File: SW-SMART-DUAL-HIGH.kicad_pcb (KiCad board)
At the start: 2 copper layers, 72 x 69 mm, 42 parts, among them IC1 MCP1416, J1 SWLINK, J2 USART1, SW1 BTS50010-1TAD, SW2 VNB35N07xx-E, U1 STM32G0B1KBTx, U4 MCP2562-E-SN

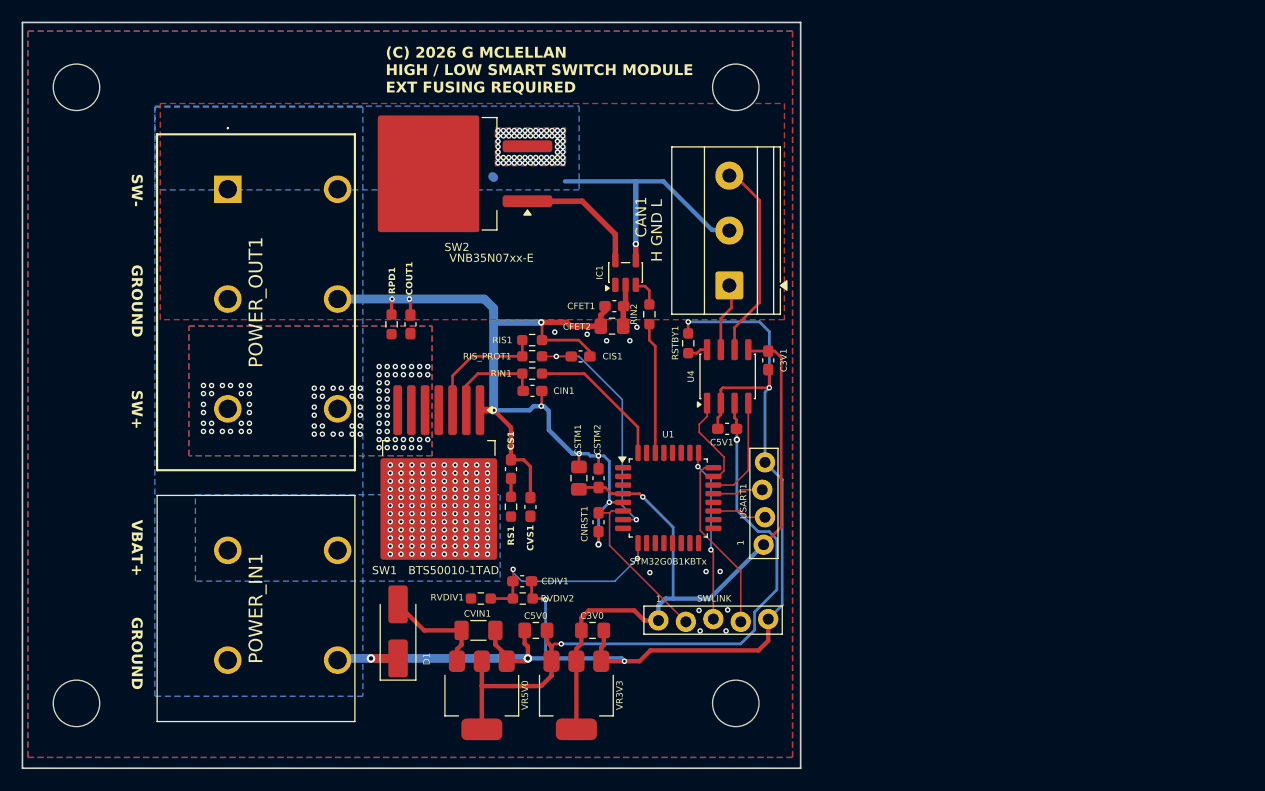
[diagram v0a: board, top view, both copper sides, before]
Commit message: lots of rework to adapt previous layout to new switch configuration
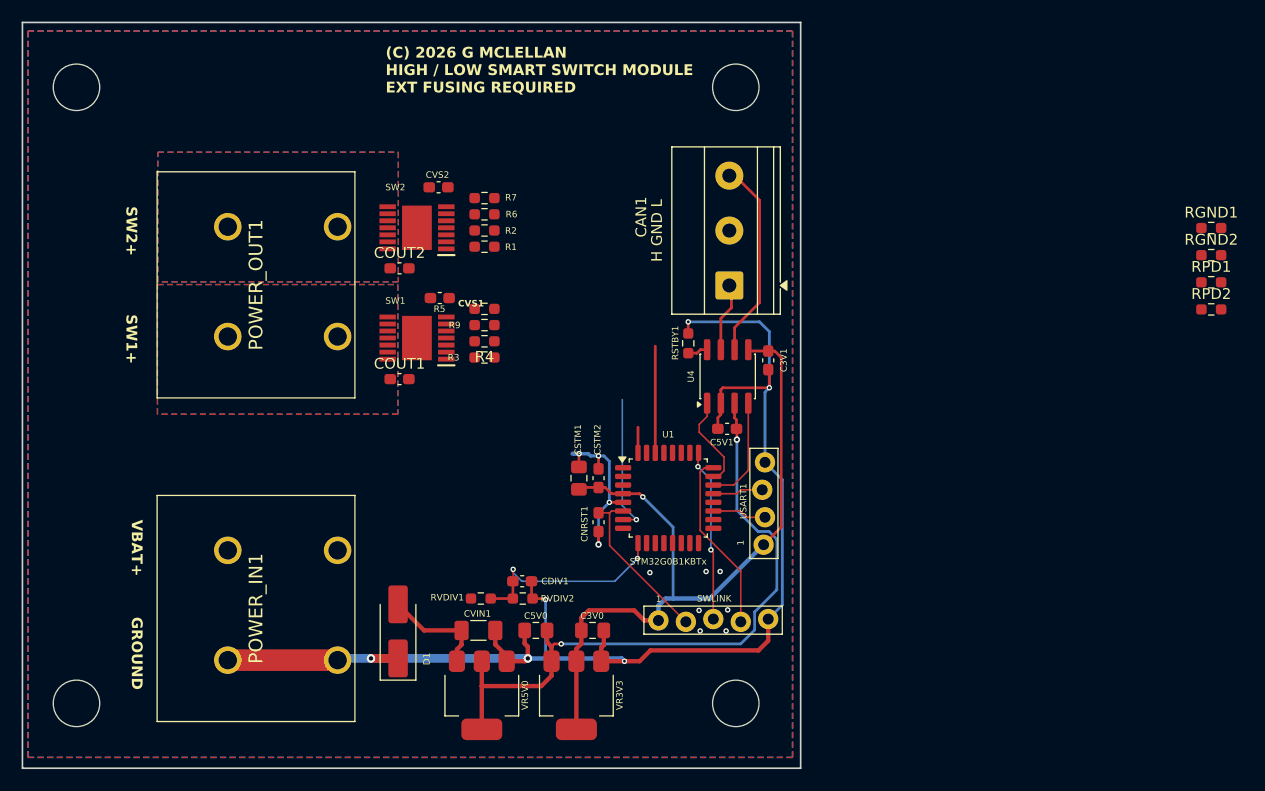
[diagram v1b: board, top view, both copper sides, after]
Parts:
- removed CFET1, CIS1: 100n, Capacitor_SMD:C_0603_1608Metric_Pad1.08x0.95mm_HandSolder
- removed CFET2: 1u, Capacitor_SMD:C_0805_2012Metric_Pad1.18x1.45mm_HandSolder
- removed CIN1: 150n, Capacitor_SMD:C_0603_1608Metric_Pad1.08x0.95mm_HandSolder
- removed the CVS1 at (128.0, 110.8)
- removed IC1: MCP1416, Package_TO_SOT_SMD:SOT-23-5
- removed RIN2: 1K0, Resistor_SMD:R_0603_1608Metric_Pad0.98x0.95mm_HandSolder
- removed RS1: 3R9, Resistor_SMD:R_0603_1608Metric_Pad0.98x0.95mm_HandSolder
- added COUT2: 10n, Capacitor_SMD:C_0603_1608Metric_Pad1.08x0.95mm_HandSolder, F.Cu at (115.9, 88.8)
- added CVS2: 68n, Capacitor_SMD:C_0603_1608Metric_Pad1.08x0.95mm_HandSolder, F.Cu at (119.5, 81.2)
- added R1: 4K7, Resistor_SMD:R_0603_1608Metric_Pad0.98x0.95mm_HandSolder, F.Cu at (123.8, 86.8)
- added R2: 4K7, Resistor_SMD:R_0603_1608Metric_Pad0.98x0.95mm_HandSolder, F.Cu at (123.8, 85.2)
- added R4: 4K7, Resistor_SMD:R_0603_1608Metric_Pad0.98x0.95mm_HandSolder, F.Cu at (123.8, 95.5)
- added R6: 10K, Resistor_SMD:R_0603_1608Metric_Pad0.98x0.95mm_HandSolder, F.Cu at (123.8, 83.8)
- added R7: 1K0, Resistor_SMD:R_0603_1608Metric_Pad0.98x0.95mm_HandSolder, F.Cu at (123.8, 82.2)
- added RGND1: 47R, Resistor_SMD:R_0603_1608Metric_Pad0.98x0.95mm_HandSolder, F.Cu at (191.0, 85.0)
- added RGND2: 47R, Resistor_SMD:R_0603_1608Metric_Pad0.98x0.95mm_HandSolder, F.Cu at (191.0, 87.5)
- added RPD2: 47K, Resistor_SMD:R_0603_1608Metric_Pad0.98x0.95mm_HandSolder, F.Cu at (191.0, 92.5)
- CVS1: renamed from CS1; value 4u7 -> 68n
- POWER_OUT1: value VP0365840000G -> SW1+ SW2+; footprint SamacSys_Parts:VP0365840000G -> SamacSys_Parts:VP0265840000G
- R5: renamed from RIS_PROT1; value 4K7 -> 10K
- RVDIV1: value 10K -> 4K7
- RVDIV2: value 4K7 -> 1K0
- SW1: value BTS50010-1TAD -> BTS7002-1EPP; footprint Package_TO_SOT_SMD:TO-263-7_TabPin4 -> SamacSys_Parts:SOP65P600X115-15N
- SW2: value VNB35N07xx-E -> BTS7002-1EPP; footprint Package_TO_SOT_SMD:TO-263-2 -> SamacSys_Parts:SOP65P600X115-15N
- moved RPD1 75.9 mm to (191.0, 90.0), turned to 0 degrees
- moved CVS1 17.1 mm to (119.6, 91.5), turned to 0 degrees
- moved SW1 14.5 mm to (117.5, 95.2), turned to 180 degrees
- moved R5 6.22 mm to (123.8, 92.5)
- moved SW2 5.62 mm to (117.5, 85.0)
- moved COUT1 5.17 mm to (115.9, 99.0), turned to 0 degrees
- moved R3 4.66 mm to (123.8, 97.0)
- moved R9 4.63 mm to (123.8, 94.0)
- moved POWER_OUT1 3.47 mm to (100.0, 84.9)
- renumbered RIN1 to R3, RIS1 to R9
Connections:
- CVS1 pad 1: Net-(CS1-Pad1) -> +12V
- POWER_OUT1 pad 3: GND -> /SW1OUT
- POWER_OUT1 pad 4: GND -> /SW1OUT
- R3 pad 1: /SW1IN -> unconnected-(R3-Pad1)
- R5 pad 1: /SW1IS -> unconnected-(R5-Pad1)
- RPD1 pad 2: /SW1OUT -> /SW2OUT
- SW1 pad 1: GND -> Net-(SW1-GND)
- SW1 pad 3: /SW1IS_PD -> Net-(SW1-DEN)
- SW1 pad 4: +12V -> /SW1IS_PD
- SW1 pad 5: /SW1OUT -> unconnected-(SW1-NC-Pad5)
- SW1 pad 6: /SW1OUT -> unconnected-(SW1-NC-Pad6)
- SW1 pad 7: /SW1OUT -> unconnected-(SW1-NC-Pad7)
- SW2 pad 1: /LOWSW -> Net-(SW2-GND)
- SW2 pad 2: /SW2OUT -> Net-(SW2-IN)
- SW2 pad 3: GND -> Net-(SW2-DEN)
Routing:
- net GND: track 225.6 -> 140.7 mm, vias 77 -> 10
- net /SW1IS_PD: track 11.9 -> 0.00 mm
- net /LOWSW: track 11.8 -> 0.00 mm
- net /SW1IN: track 13.3 -> 2.38 mm
- net /SW1IS: track 23.3 -> 12.9 mm, vias 2 -> 1
- net Net-(SW1-IN): track 9.56 -> 0.00 mm
- net +12V: track 17.8 -> 9.90 mm, vias 132 -> 7
- net Net-(IC1-IN): track 2.75 -> 0.00 mm
- net /SW2IN: track 12.1 -> 9.88 mm
- net Net-(CS1-Pad1): track 1.70 -> 0.00 mm
- net /SW1OUT: vias 89 -> 0
- added copper zone on B.Cu, net /SW2OUT
- removed copper zone on B.Cu, net GND
- removed copper zone on F.Cu, net GND
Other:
- board text added: "SW1+"
- board text added: "SW2+"
- board text removed: "SW+"
- board text removed: "SW-"

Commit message: fix supply plane pour alignment
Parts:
- POWER_OUT1: value SW1+ SW2+ -> ~; footprint SamacSys_Parts:VP0265840000G -> TerminalBlock_Phoenix:TerminalBlock_Phoenix_MKDS-1,5-3-5.08_1x03_P5.08mm_Horizontal
- moved RPD2 76.6 mm to (114.8, 100.3), turned to 180 degrees
- moved RPD1 76.2 mm to (114.8, 88.9), turned to 180 degrees
- moved RGND1 68.6 mm to (123.8, 98.5)
- moved RGND2 67.2 mm to (123.8, 86.9)
- moved RVDIV2 4.16 mm to (123.4, 117.8), turned to 0 degrees
- moved CDIV1 4.07 mm to (123.4, 116.3), turned to 180 degrees
- moved CVS2 2.56 mm to (121.3, 79.4)
- moved CVS1 1.80 mm to (121.3, 91.0)
- moved COUT2 1.77 mm to (114.8, 87.4)
- moved R1 1.35 mm to (123.8, 85.4)
- moved R2 1.35 mm to (123.8, 83.9)
- moved R6 1.35 mm to (123.8, 82.4)
- moved R7 1.35 mm to (123.8, 80.9)
- moved SW2 1.20 mm to (117.6, 83.8)
- moved COUT1 1.15 mm to (114.8, 98.8)
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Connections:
- POWER_OUT1 pad 2: /SW2OUT -> unconnected-(POWER_OUT1-Pin_2-Pad2)
- R1 pad 1: unconnected-(R1-Pad1) -> /SW2IN
- R2 pad 1: unconnected-(R2-Pad1) -> /SW2DEN
- R3 pad 1: unconnected-(R3-Pad1) -> /SW1IN
- R4 pad 1: unconnected-(R4-Pad1) -> /SW1DEN
- R5 pad 1: unconnected-(R5-Pad1) -> /SW1IS
- R6 pad 1: unconnected-(R6-Pad1) -> /SW2IS
- U1 pad 29: unconnected-(U1-PB5-Pad29) -> /SW2DEN
- U1 pad 31: unconnected-(U1-PB7-Pad31) -> /SW1DEN
- U1 pad 8: unconnected-(U1-PA1-Pad8) -> /SW2IS
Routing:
- net GND: track 140.7 -> 88.0 mm, vias 10 -> 19
- net /SW2IS: track 0.00 -> 39.5 mm, vias 0 -> 2
- net /SW2DEN: track 0.00 -> 32.8 mm
- net /SW2IN: track 9.88 -> 31.1 mm
- net /SW1DEN: track 0.00 -> 20.8 mm
- net /SW1IS: track 12.9 -> 30.6 mm, vias 1 -> 2
- net /SW1IN: track 2.38 -> 19.0 mm
- net +12V: track 9.90 -> 3.03 mm, vias 7 -> 80
- net /SW2IS_PD: track 0.00 -> 4.94 mm
- net /SW1IS_PD: track 0.00 -> 4.62 mm
- net Net-(SW1-GND): track 0.00 -> 3.18 mm
- net Net-(SW2-GND): track 0.00 -> 3.02 mm
- net Net-(SW2-DEN): track 0.00 -> 2.96 mm
- net Net-(SW1-IN): track 0.00 -> 2.83 mm
- net Net-(SW2-IN): track 0.00 -> 2.81 mm
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- added copper zone on B.Cu, net GND
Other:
- board text added: "(C) 2026 G MCLELLAN DUAL HIGH SIDE SMART SWITCH EXT FUSING REQUIRED"
- board text removed: "(C) 2026 G MCLELLAN HIGH / LOW SMART SWITCH MODULE EXT FUSING REQUIRED"
